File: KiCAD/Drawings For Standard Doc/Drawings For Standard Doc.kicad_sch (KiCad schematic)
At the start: 0 parts

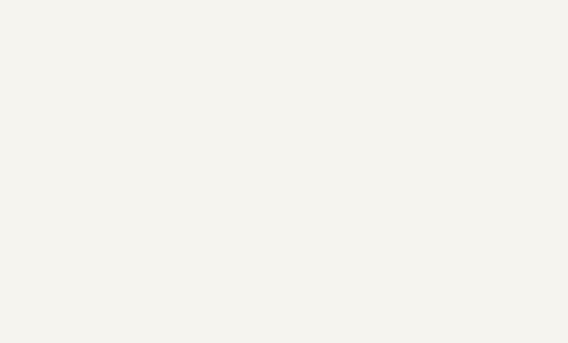
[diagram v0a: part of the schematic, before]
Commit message: https://github.com/Halibut-Electronics/Open-Headset-Interconnect-Standard/issues/3 Adding Dynamic Mic Preamp circuit.
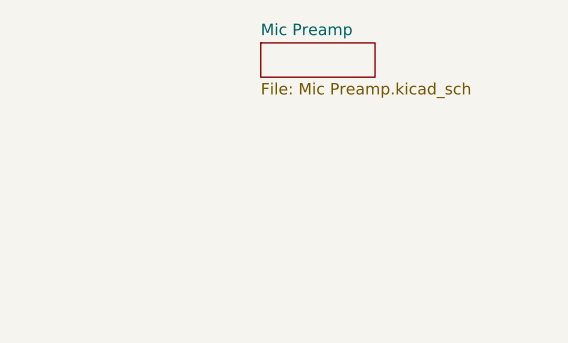
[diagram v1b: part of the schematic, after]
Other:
- added sheet Mic Preamp (Mic Preamp.kicad_sch)
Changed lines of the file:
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@@
+    )
+  )
+  (sheet (at 142.875 132.715) (size 12.7 3.81) (fields_autoplaced)
+    (stroke (width 0.1524) (type solid) (color 0 0 0 0))
+    (fill (color 0 0 0 0.0000))
+    (property "Sheet name" "Mic Preamp" (id 0) (at 142.875 132.0034 0)
+      (effects (font (size 1.27 1.27)) (justify left bottom))
+    )
+    (property "Sheet file" "Mic Preamp.kicad_sch" (id 1) (at 142.875 137.1096 0)
+      (effects (font (size 1.27 1.27)) (justify left top))
     )
   )
@@
     (path "/37aa262a-aeff-44bf-a2ca-eead12de1830" (page "3"))
     (path "/71cdc780-190f-4121-90aa-59d0facb45e7" (page "4"))
+    (path "/ca44b5d4-9a6d-4dee-93ca-025d4c948068" (page "5"))
   )
   (symbol_instances
+    (path "/ca44b5d4-9a6d-4dee-93ca-025d4c948068/b38be19c-4a55-4485-a72a-966d70e9e8b9"
+      (reference "#PWR?") (unit 1) (value "+5V") (footprint "")
+    )
+    (path "/ca44b5d4-9a6d-4dee-93ca-025d4c948068/dd17bc22-04c3-49ee-9776-22149b4ebecb"
+      (reference "#PWR?") (unit 1) (value "GND") (footprint "")
+    )
+    (path "/ca44b5d4-9a6d-4dee-93ca-025d4c948068/87b6f75a-b017-4a5d-a9b4-b7c18cb96788"
+      (reference "C1") (unit 1) (value "1uF") (footprint "")
+    )
+    (path "/ca44b5d4-9a6d-4dee-93ca-025d4c948068/232358ed-2354-4b9d-bcbd-a4e9e13dee87"
+      (reference "C?") (unit 1) (value "1uF") (footprint "")
+    )
+    (path "/ca44b5d4-9a6d-4dee-93ca-025d4c948068/763466a8-7a39-4d18-8dc4-edf1e9800158"
+      (reference "C?") (unit 1) (value "1uF") (footprint "Capacitor_SMD:C_0603_1608Metric_Pad1.08x0.95mm_HandSolder")
+    )
     (path "/71cdc780-190f-4121-90aa-59d0facb45e7/293e1602-9b03-42d6-9153-8377027028aa"
       (reference "J?") (unit 1) (value "Headphones") (footprint "")
@@
       (reference "MK?") (unit 1) (value "Microphone") (footprint "")
     )
+    (path "/ca44b5d4-9a6d-4dee-93ca-025d4c948068/b27f371b-229e-47b3-94ce-3c61765fb8d3"
+      (reference "MK?") (unit 1) (value "Dynamic Microphone") (footprint "")
+    )
     (path "/37aa262a-aeff-44bf-a2ca-eead12de1830/d2076957-2817-4b19-b10b-5f6536800f05"
       (reference "MK?") (unit 1) (value "Electret") (footprint "")
     )
+    (path "/ca44b5d4-9a6d-4dee-93ca-025d4c948068/fd41e53f-953a-40c3-8c37-cdfc390b6686"
+      (reference "Q1") (unit 1) (value "S9013") (footprint "Package_TO_SOT_SMD:SOT-23")
+    )
+    (path "/ca44b5d4-9a6d-4dee-93ca-025d4c948068/b0ddad96-0c7b-4f69-89e3-9821faaeba76"
+      (reference "Q?") (unit 1) (value "S9013") (footprint "Package_TO_SOT_SMD:SOT-23")
+    )
+    (path "/ca44b5d4-9a6d-4dee-93ca-025d4c948068/9a6e82d0-de0c-414f-8e45-41fbd86323ce"
+      (reference "R1") (unit 1) (value "75k") (footprint "")
+    )
+    (path "/ca44b5d4-9a6d-4dee-93ca-025d4c948068/d699ee28-09f1-49fe-8617-a9b88e969a51"
+      (reference "R2") (unit 1) (value "27k") (footprint "")
+    )
+    (path "/ca44b5d4-9a6d-4dee-93ca-025d4c948068/0385a075-452b-4a8f-b9e7-d37180115693"
+      (reference "R3") (unit 1) (value "470") (footprint "")
+    )
+    (path "/ca44b5d4-9a6d-4dee-93ca-025d4c948068/1f9535e3-49ca-43d0-8b41-e73852bb1280"
+      (reference "R?") (unit 1) (value "75k") (footprint "Resistor_SMD:R_0603_1608Metric_Pad0.98x0.95mm_HandSolder")
+    )
+    (path "/ca44b5d4-9a6d-4dee-93ca-025d4c948068/91b59feb-7114-4152-b2aa-12628cebf4c8"
+      (reference "R?") (unit 1) (value "2.2k") (footprint "")
+    )
+    (path "/ca44b5d4-9a6d-4dee-93ca-025d4c948068/af5e3980-fd77-42d1-b371-312cf282047e"
+      (reference "R?") (unit 1) (value "27k") (footprint "Resistor_SMD:R_0603_1608Metric_Pad0.98x0.95mm_HandSolder")
+    )
+    (path "/ca44b5d4-9a6d-4dee-93ca-025d4c948068/e8af02bf-a491-4eee-b76b-b834b657eb34"
+      (reference "R?") (unit 1) (value "470") (footprint "Resistor_SMD:R_0603_1608Metric_Pad0.98x0.95mm_HandSolder")
+    )
     (path "/37aa262a-aeff-44bf-a2ca-eead12de1830/078b4861-02f9-41dc-a2e8-a190a6ad9f92"

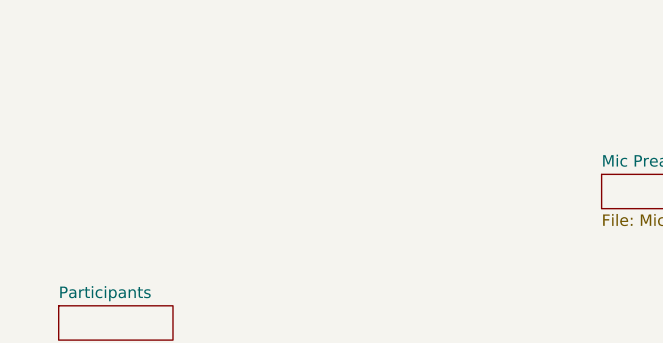
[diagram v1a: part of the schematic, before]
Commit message: First draft of QSO Today Expo presentation.
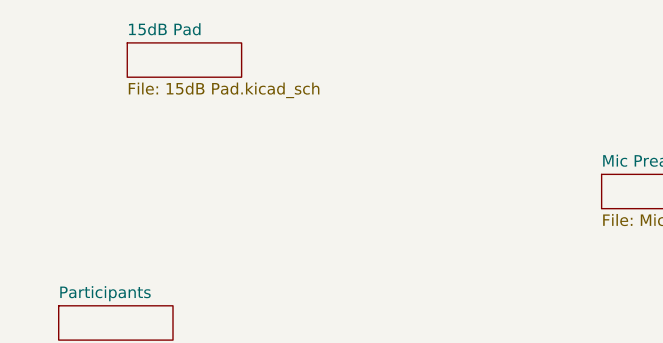
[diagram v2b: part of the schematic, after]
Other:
- added sheet 15dB Pad (15dB Pad.kicad_sch)
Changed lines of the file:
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@@
+    )
+  )
+  (sheet (at 90.17 118.11) (size 12.7 3.81) (fields_autoplaced)
+    (stroke (width 0.1524) (type solid) (color 0 0 0 0))
+    (fill (color 0 0 0 0.0000))
+    (property "Sheet name" "15dB Pad" (id 0) (at 90.17 117.3984 0)
+      (effects (font (size 1.27 1.27)) (justify left bottom))
+    )
+    (property "Sheet file" "15dB Pad.kicad_sch" (id 1) (at 90.17 122.5046 0)
+      (effects (font (size 1.27 1.27)) (justify left top))
     )
   )
@@
     (path "/71cdc780-190f-4121-90aa-59d0facb45e7" (page "4"))
     (path "/ca44b5d4-9a6d-4dee-93ca-025d4c948068" (page "5"))
+    (path "/590b8635-2deb-410e-a711-8e6a6ccf9070" (page "6"))
   )
   (symbol_instances
+    (path "/590b8635-2deb-410e-a711-8e6a6ccf9070/99f00e9f-dd0f-45db-b64c-f25c3dc4fd9e"
+      (reference "#PWR?") (unit 1) (value "+5V") (footprint "")
+    )
     (path "/ca44b5d4-9a6d-4dee-93ca-025d4c948068/b38be19c-4a55-4485-a72a-966d70e9e8b9"
       (reference "#PWR?") (unit 1) (value "+5V") (footprint "")
@@
     (path "/ca44b5d4-9a6d-4dee-93ca-025d4c948068/763466a8-7a39-4d18-8dc4-edf1e9800158"
       (reference "C?") (unit 1) (value "1uF") (footprint "Capacitor_SMD:C_0603_1608Metric_Pad1.08x0.95mm_HandSolder")
+    )
+    (path "/590b8635-2deb-410e-a711-8e6a6ccf9070/996a8da4-b4ce-4604-ae41-6002928d0504"
+      (reference "C?") (unit 1) (value "1uF") (footprint "")
     )
     (path "/71cdc780-190f-4121-90aa-59d0facb45e7/293e1602-9b03-42d6-9153-8377027028aa"
@@
       (reference "R3") (unit 1) (value "470") (footprint "")
     )
+    (path "/590b8635-2deb-410e-a711-8e6a6ccf9070/0013e5d4-135e-4c61-a5df-1fd2721df2c6"
+      (reference "R?") (unit 1) (value "2.2k") (footprint "")
+    )
+    (path "/590b8635-2deb-410e-a711-8e6a6ccf9070/0857fd1d-0abe-4bf2-a523-7d6e6c34fafe"
+      (reference "R?") (unit 1) (value "100") (footprint "")
+    )
     (path "/ca44b5d4-9a6d-4dee-93ca-025d4c948068/1f9535e3-49ca-43d0-8b41-e73852bb1280"
       (reference "R?") (unit 1) (value "75k") (footprint "Resistor_SMD:R_0603_1608Metric_Pad0.98x0.95mm_HandSolder")
     )
+    (path "/590b8635-2deb-410e-a711-8e6a6ccf9070/466e6237-2a48-4347-bfb6-e604f797e4c0"
+      (reference "R?") (unit 1) (value "1.5k") (footprint "")
+    )
     (path "/ca44b5d4-9a6d-4dee-93ca-025d4c948068/91b59feb-7114-4152-b2aa-12628cebf4c8"
